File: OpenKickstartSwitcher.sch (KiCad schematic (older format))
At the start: 12 parts, among them J1 Conn_01x03, J2 Conn_01x03, J99 OSHW_LOGO, U1 KS_SOCKET, U2 M27C800, U3 7400

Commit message: Almost ready for V2
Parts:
- removed J2: Conn_01x03, OpenKickstartSwitcher:LoosePads-3, symbol Conn_01x03
- added J2: Conn_01x04, OpenKickstartSwitcher:LoosePads-4, symbol Conn_01x04
- added J3: A19, OpenKickstartSwitcher:LoosePads-1, symbol Conn_01x01
- R1, R2: footprint Resistors_THT:R_Axial_DIN0207_L6.3mm_D2.5mm_P10.16mm_Horizontal -> Resistors_THT:R_Axial_DIN0207_L6.3mm_D2.5mm_P7.62mm_Horizontal
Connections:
- net GND: now also J2.3 (Pin_3)
- net VCC: now also J2.4 (Pin_4)
- net sw17: now also J2.2 (Pin_2)
- net sw18: now also J2.1 (Pin_1)
- net at U2.42 ((A19)): now also J3.1 (Pin_1)
- no-connect marks 4 -> 3
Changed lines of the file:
@@
 Sheet 1 1
 Title "OpenKickstartSwitcher"
-Date "2018-01-07"
-Rev "1"
+Date "2018-04-10"
+Rev "2"
 Comp "SukkoPera"
 Comment1 "Inspired from work by Henryk Richter"
@@
 	1    0    0    -1
 $EndComp
-NoConn ~ 8875 3150
 $Comp
 L AMIGA_ROM U1
@@
 $EndComp
 $Comp
-L Conn_01x03 J2
-U 1 1 5A2F23BB
-P 2075 1500
-F 0 "J2" H 2075 1700 50  0000 C CNN
-F 1 "Conn_01x03" H 2075 1300 50  0001 C CNN
-F 2 "OpenKickstartSwitcher:LoosePads-3" H 2075 1500 50  0001 C CNN
-F 3 "" H 2075 1500 50  0001 C CNN
-	1    2075 1500
-	-1   0    0    -1
-$EndComp
-$Comp
 L R R1
 U 1 1 5A2F3104
@@
 F 0 "R1" V 2430 1125 50  0000 C CNN
 F 1 "10k" V 2350 1125 50  0000 C CNN
-F 2 "Resistors_THT:R_Axial_DIN0207_L6.3mm_D2.5mm_P10.16mm_Horizontal" V 2280 1125 50  0001 C CNN
+F 2 "Resistors_THT:R_Axial_DIN0207_L6.3mm_D2.5mm_P7.62mm_Horizontal" V 2280 1125 50  0001 C CNN
 F 3 "" H 2350 1125 50  0001 C CNN
 	1    2350 1125
@@
 F 0 "R2" V 2630 1125 50  0000 C CNN
 F 1 "10k" V 2550 1125 50  0000 C CNN
-F 2 "Resistors_THT:R_Axial_DIN0207_L6.3mm_D2.5mm_P10.16mm_Horizontal" V 2480 1125 50  0001 C CNN
+F 2 "Resistors_THT:R_Axial_DIN0207_L6.3mm_D2.5mm_P7.62mm_Horizontal" V 2480 1125 50  0001 C CNN
 F 3 "" H 2550 1125 50  0001 C CNN
 	1    2550 1125
@@
 	10850 800  10850 950
 Wire Wire Line
-	2275 1600 2350 1600
+	2050 1600 2350 1600
 Wire Wire Line
 	2350 1600 2350 1700
 Wire Wire Line
-	2275 1400 2775 1400
+	2050 1400 2775 1400
 Wire Wire Line
 	2775 1275 2775 2825
@@
 	5925 1925 5825 1925
 Wire Wire Line
-	2275 1500 2975 1500
+	2050 1500 2975 1500
 Wire Wire Line
 	2975 1500 2975 2150
@@
 	3175 1925 3325 1925
 Wire Wire Line
-	2350 875  3175 875
+	2150 875  3175 875
 Wire Wire Line
 	2350 875  2350 975
@@
 Text Label 2875 1075 0    60   ~ 0
 a17
+$Comp
+L Conn_01x04 J2
+U 1 1 5ACCFC51
+P 1850 1500
+F 0 "J2" H 1850 1700 50  0000 C CNN
+F 1 "Conn_01x04" H 1850 1200 50  0001 C CNN
+F 2 "OpenKickstartSwitcher:LoosePads-4" H 1850 1500 50  0001 C CNN
+F 3 "" H 1850 1500 50  0001 C CNN
+	1    1850 1500
+	-1   0    0    -1
+$EndComp
+Wire Wire Line
+	2050 1700 2150 1700
+Wire Wire Line
+	2150 1700 2150 875
+Connection ~ 2350 875
+$Comp
+L Conn_01x01 J3
+U 1 1 5ACD0463
+P 9075 2775
+F 0 "J3" H 9075 2875 50  0000 C CNN
+F 1 "A19" H 9075 2675 50  0000 C CNN
+F 2 "OpenKickstartSwitcher:LoosePads-1" H 9075 2775 50  0001 C CNN
+F 3 "" H 9075 2775 50  0001 C CNN
+	1    9075 2775
+	0    -1   -1   0
+$EndComp
+Wire Wire Line
+	8875 3150 9075 3150
+Wire Wire Line
+	9075 3150 9075 2975
 $EndSCHEMATC

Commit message: Use smaller footprint for resistors
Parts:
- R1, R2: footprint Resistors_THT:R_Axial_DIN0207_L6.3mm_D2.5mm_P7.62mm_Horizontal -> Resistors_THT:R_Axial_DIN0204_L3.6mm_D1.6mm_P7.62mm_Horizontal
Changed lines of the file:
@@
 F 0 "R1" V 2430 1125 50  0000 C CNN
 F 1 "10k" V 2350 1125 50  0000 C CNN
-F 2 "Resistors_THT:R_Axial_DIN0207_L6.3mm_D2.5mm_P7.62mm_Horizontal" V 2280 1125 50  0001 C CNN
+F 2 "Resistors_THT:R_Axial_DIN0204_L3.6mm_D1.6mm_P7.62mm_Horizontal" V 2280 1125 50  0001 C CNN
 F 3 "" H 2350 1125 50  0001 C CNN
 	1    2350 1125
@@
 F 0 "R2" V 2630 1125 50  0000 C CNN
 F 1 "10k" V 2550 1125 50  0000 C CNN
-F 2 "Resistors_THT:R_Axial_DIN0207_L6.3mm_D2.5mm_P7.62mm_Horizontal" V 2480 1125 50  0001 C CNN
+F 2 "Resistors_THT:R_Axial_DIN0204_L3.6mm_D1.6mm_P7.62mm_Horizontal" V 2480 1125 50  0001 C CNN
 F 3 "" H 2550 1125 50  0001 C CNN
 	1    2550 1125

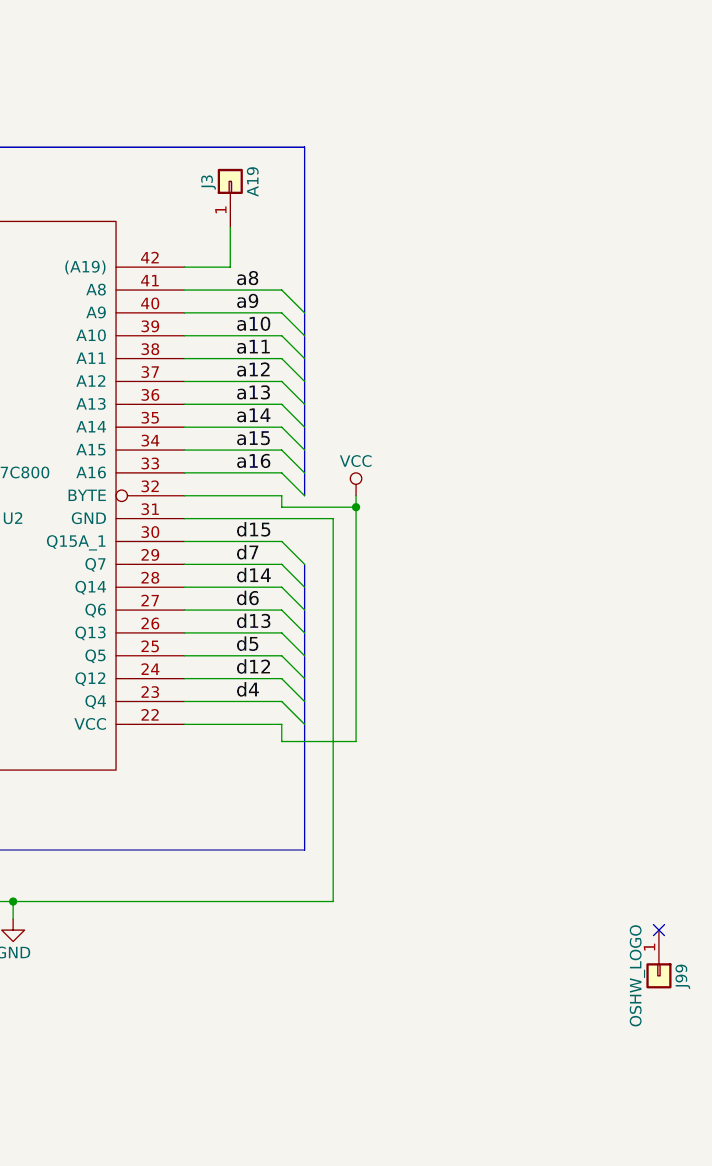
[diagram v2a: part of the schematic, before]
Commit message: Replace SW3 with a solder jumper
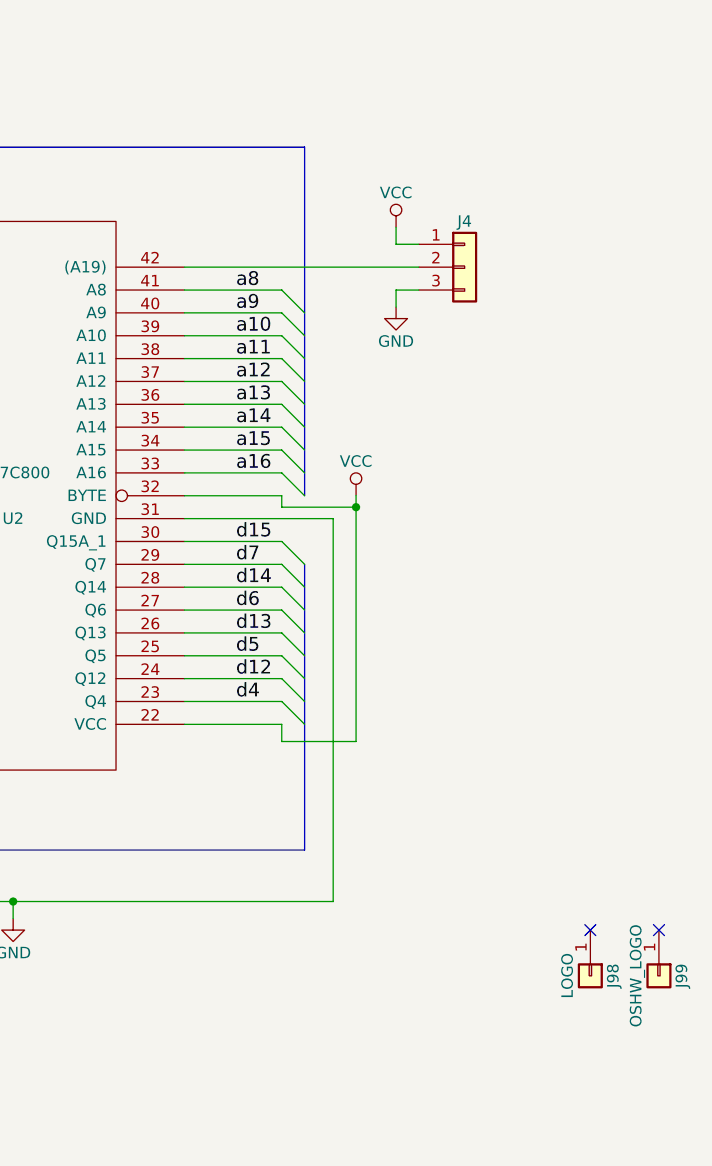
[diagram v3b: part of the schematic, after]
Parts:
- removed J3: A19, OpenKickstartSwitcher:LoosePads-1, symbol Conn_01x01
- added J4: Conn_01x03, OpenKickstartSwitcher:SolderJumper, symbol Conn_01x03
- added J98: LOGO, logo:logo, symbol Conn_01x01
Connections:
- net GND: now also J4.3 (Pin_3)
- net VCC: now also J4.1 (Pin_1)
- net at U2.42 ((A19)): now also J4.2 (Pin_2)
- no-connect marks 3 -> 4
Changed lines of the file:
@@
 Sheet 1 1
 Title "OpenKickstartSwitcher"
-Date "2018-04-10"
+Date "2018-04-12"
 Rev "2"
 Comp "SukkoPera"
@@
 	2150 1700 2150 875
 Connection ~ 2350 875
-$Comp
-L Conn_01x01 J3
-U 1 1 5ACD0463
-P 9075 2775
-F 0 "J3" H 9075 2875 50  0000 C CNN
-F 1 "A19" H 9075 2675 50  0000 C CNN
-F 2 "OpenKickstartSwitcher:LoosePads-1" H 9075 2775 50  0001 C CNN
-F 3 "" H 9075 2775 50  0001 C CNN
-	1    9075 2775
-	0    -1   -1   0
-$EndComp
-Wire Wire Line
-	8875 3150 9075 3150
-Wire Wire Line
-	9075 3150 9075 2975
+Wire Wire Line
+	8875 3150 9900 3150
+$Comp
+L Conn_01x03 J4
+U 1 1 5ACFB332
+P 10100 3150
+F 0 "J4" H 10100 3350 50  0000 C CNN
+F 1 "Conn_01x03" H 10100 2950 50  0001 C CNN
+F 2 "OpenKickstartSwitcher:SolderJumper" H 10100 3150 50  0001 C CNN
+F 3 "" H 10100 3150 50  0001 C CNN
+	1    10100 3150
+	1    0    0    -1
+$EndComp
+$Comp
+L VCC #PWR013
+U 1 1 5ACFB9D7
+P 9800 2975
+F 0 "#PWR013" H 9800 2825 50  0001 C CNN
+F 1 "VCC" H 9800 3125 50  0000 C CNN
+F 2 "" H 9800 2975 50  0001 C CNN
+F 3 "" H 9800 2975 50  0001 C CNN
+	1    9800 2975
+	1    0    0    -1
+$EndComp
+Wire Wire Line
+	9800 2975 9800 3050
+Wire Wire Line
+	9800 3050 9900 3050
+$Comp
+L GND #PWR014
+U 1 1 5ACFBBEC
+P 9800 3325
+F 0 "#PWR014" H 9800 3075 50  0001 C CNN
+F 1 "GND" H 9800 3175 50  0000 C CNN
+F 2 "" H 9800 3325 50  0001 C CNN
+F 3 "" H 9800 3325 50  0001 C CNN
+	1    9800 3325
+	1    0    0    -1
+$EndComp
+Wire Wire Line
+	9800 3325 9800 3250
+Wire Wire Line
+	9800 3250 9900 3250
+$Comp
+L Conn_01x01 J98
+U 1 1 5ACFCA75
+P 10650 6250
+F 0 "J98" H 10650 6350 50  0000 C CNN
+F 1 "LOGO" H 10650 6150 50  0000 C CNN
+F 2 "logo:logo" H 10650 6250 50  0001 C CNN
+F 3 "" H 10650 6250 50  0001 C CNN
+	1    10650 6250
+	0    1    1    0
+$EndComp
+NoConn ~ 10650 6050
 $EndSCHEMATC

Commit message: Initial commit of CDTV version - NOT READY YET
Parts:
- C1, C2: footprint Capacitors_THT:C_Disc_D7.0mm_W2.5mm_P5.00mm -> Capacitor_THT:C_Disc_D7.0mm_W2.5mm_P5.00mm; symbol C -> OpenKickstartSwitcher-rescue:C
- J1, J4: symbol Conn_01x03 -> OpenKickstartSwitcher-rescue:Conn_01x03
- J2: footprint OpenKickstartSwitcher:LoosePads-4 -> OpenKickstartSwitcher:Solderable_PinHeader_1x04; symbol Conn_01x04 -> OpenKickstartSwitcher-rescue:Conn_01x04
- J98, J99: symbol Conn_01x01 -> OpenKickstartSwitcher-rescue:Conn_01x01
- R1, R2: footprint Resistors_THT:R_Axial_DIN0204_L3.6mm_D1.6mm_P7.62mm_Horizontal -> Resistor_THT:R_Axial_DIN0204_L3.6mm_D1.6mm_P7.62mm_Horizontal; symbol R -> OpenKickstartSwitcher-rescue:R
- RN1, RN2: footprint Resistors_THT:R_Array_SIP10 -> Resistor_THT:R_Array_SIP10; symbol R_Network09 -> OpenKickstartSwitcher-rescue:R_Network09
- U1: symbol AMIGA_ROM -> AMIGA_ROM:AMIGA_ROM
- U2: symbol M27C800 -> OpenKickstartSwitcher:M27C800
- U3: footprint Housings_DIP:DIP-14_W7.62mm -> Package_DIP:DIP-14_W7.62mm_Socket; symbol 7400 -> OpenKickstartSwitcher-rescue:7400
